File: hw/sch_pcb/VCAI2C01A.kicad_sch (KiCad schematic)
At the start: 74 parts, among them J10 JUMP2_2x1, J11 JUMP2_2x1, J13 JUMP_5X2, J14 JUMP_2x1, J15 JUMP_2x1, J16 JUMP_2x1, J17 JUMP_2x1, J18 JUMP_2x1, J19 JUMP_2x1, J2 CONN_2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

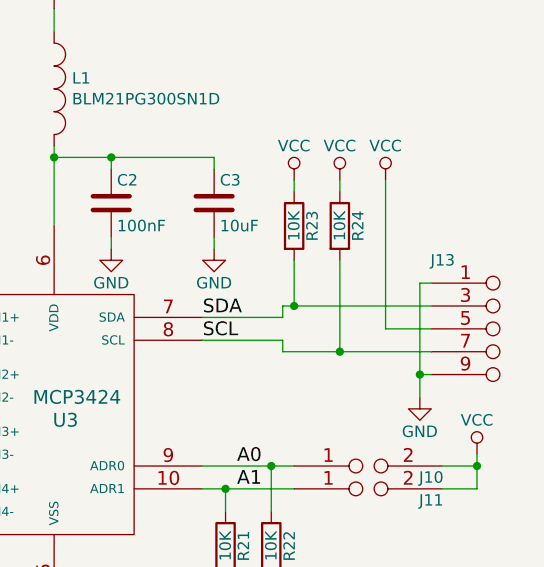
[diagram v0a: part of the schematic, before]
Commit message: Cleanup copper pour layout. Add powerflags to schematics.
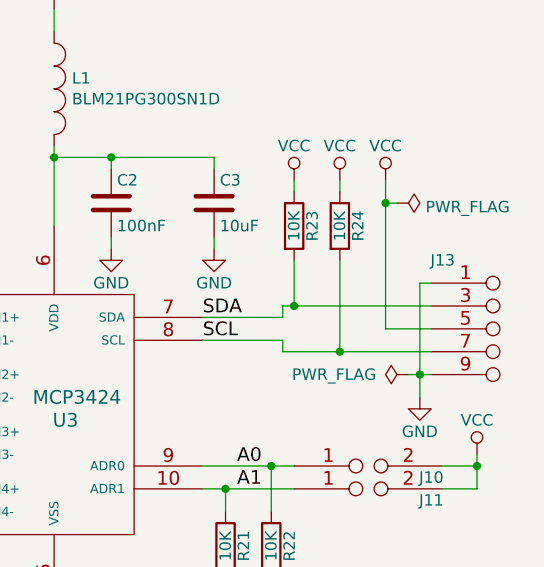
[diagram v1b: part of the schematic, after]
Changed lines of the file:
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@@
   (junction (at 165.1 46.99) (diameter 0) (color 0 0 0 0)
   )
+  (junction (at 264.16 105.41) (diameter 0) (color 0 0 0 0)
+  )
   (junction (at 208.28 127) (diameter 0) (color 0 0 0 0)
   )
@@
     (stroke (width 0) (type default) (color 0 0 0 0))
   )
+  (wire (pts (xy 266.7 124.46) (xy 267.97 124.46))
+    (stroke (width 0) (type default) (color 0 0 0 0))
+  )
   (wire (pts (xy 138.43 101.6) (xy 148.59 101.6))
     (stroke (width 0) (type default) (color 0 0 0 0))
@@
     (stroke (width 0) (type default) (color 0 0 0 0))
   )
+  (wire (pts (xy 264.16 105.41) (xy 264.16 119.38))
+    (stroke (width 0) (type default) (color 0 0 0 0))
+  )
   (wire (pts (xy 44.45 105.41) (xy 44.45 111.76))
     (stroke (width 0) (type default) (color 0 0 0 0))
@@
     (stroke (width 0) (type default) (color 0 0 0 0))
   )
-  (wire (pts (xy 264.16 102.87) (xy 264.16 119.38))
+  (wire (pts (xy 264.16 102.87) (xy 264.16 105.41))
     (stroke (width 0) (type default) (color 0 0 0 0))
   )
@@
   )
   (wire (pts (xy 146.05 38.1) (xy 146.05 48.26))
+    (stroke (width 0) (type default) (color 0 0 0 0))
+  )
+  (wire (pts (xy 264.16 105.41) (xy 265.43 105.41))
     (stroke (width 0) (type default) (color 0 0 0 0))
   )
@@
     (pin "1")
   )
+  (symbol (lib_id "power:PWR_FLAG") (at 265.43 105.41 270) (unit 1)
+    (in_bom yes) (on_board yes) (fields_autoplaced)
+    (property "Reference" "#FLG0102" (id 0) (at 267.335 105.41 0)
+      (effects (font (size 1.27 1.27)) hide)
+    )
+    (property "Value" "PWR_FLAG" (id 1) (at 268.605 105.8438 90)
+      (effects (font (size 1.27 1.27)) (justify left))
+    )
+    (property "Footprint" "" (id 2) (at 265.43 105.41 0)
+      (effects (font (size 1.27 1.27)) hide)
+    )
+    (property "Datasheet" "~" (id 3) (at 265.43 105.41 0)
+      (effects (font (size 1.27 1.27)) hide)
+    )
+    (pin "1")
+  )
+  (symbol (lib_id "power:PWR_FLAG") (at 266.7 124.46 90) (unit 1)
+    (in_bom yes) (on_board yes)
+    (property "Reference" "#FLG0101" (id 0) (at 264.795 124.46 0)
+      (effects (font (size 1.27 1.27)) hide)
+    )
+    (property "Value" "PWR_FLAG" (id 1) (at 258.445 124.46 90))
+    (property "Footprint" "" (id 2) (at 266.7 124.46 0)
+      (effects (font (size 1.27 1.27)) hide)
+    )
+    (property "Datasheet" "~" (id 3) (at 266.7 124.46 0)
+      (effects (font (size 1.27 1.27)) hide)
+    )
+    (pin "1")
+  )
   (sheet_instances
     (path "/" (page "1"))
   )
   (symbol_instances
+    (path "/cfa6dccb-d1e3-434c-8cf7-89b011bc7d2d"
+      (reference "#FLG0101") (unit 1) (value "PWR_FLAG") (footprint "")
+    )
+    (path "/7b6b7e87-ac60-4847-bef9-1ed663b1500b"
+      (reference "#FLG0102") (unit 1) (value "PWR_FLAG") (footprint "")
+    )
     (path "/00000000-0000-0000-0000-000057d2636a"
       (reference "#PWR01") (unit 1) (value "VCC") (footprint "")
